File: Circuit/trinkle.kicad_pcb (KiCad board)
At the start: 2 copper layers, 13.6 x 23.2 mm, 12 parts, among them IC1 ATTINY84A-SS, P1 ISCP, P2 CONN_7, P3 CONN_7, SW1 RESET

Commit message: Photos and readme update
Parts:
- C2: value 10u -> 1u
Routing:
- net N-0000013: track 17.2 -> 17.9 mm
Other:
- board text added: "Trinkle ATTiny 84 Breakout - Version 1.1 Designed by John Spencer, 2014 https://github.com/mage0r/trinkle Made at hackmelbourne.org"
- board text removed: "Trinkle - ATTiny 84 Breakout Designed by John Spencer, 2014 https://github.com/mage0r/trinkle Version 1.0"
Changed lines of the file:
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@@
     (links 34)
     (no_connects 0)
-    (area 6.45 10.5264 27.3026 38)
+    (area 7.15 10.5264 27.3026 38.9)
     (thickness 1.6)
-    (drawings 25)
+    (drawings 27)
     (tracks 147)
     (zones 0)
@@
     (pad_to_mask_clearance 0)
     (aux_axis_origin 0 0)
-    (visible_elements FFFFFFBF)
+    (visible_elements 7FFFFFFF)
     (pcbplotparams
       (layerselection 284196865)
@@
       (effects (font (size 0.508 0.4572) (thickness 0.1143)))
     )
-    (fp_text value 10u (at 0 1 270) (layer F.SilkS)
+    (fp_text value 1u (at 0 1 270) (layer F.SilkS)
       (effects (font (size 0.4 0.4) (thickness 0.1)))
     )
@@
       (effects (font (size 0.7493 0.7493) (thickness 0.14986)))
     )
-    (fp_text value ATTINY84A-SS (at 0 1 90) (layer F.SilkS)
+    (fp_text value ATTINY84A-SS (at 0 0 90) (layer F.SilkS)
       (effects (font (size 0.7493 0.7493) (thickness 0.14986)))
     )
@@
     )
   )
-  (gr_text "Trinkle - ATTiny 84 Breakout\nDesigned by John Spencer, 2014\nhttps://github.com/mage0r/trinkle\nVersion 1.0" (at 20 35.2 270) (layer B.SilkS)
+  (gr_text +5V (at 21.9 35.2) (layer F.SilkS)
+    (effects (font (size 0.5 0.5) (thickness 0.125)))
+  )
+  (gr_text GND (at 16.5 35.2) (layer F.SilkS)
+    (effects (font (size 0.5 0.5) (thickness 0.125)))
+  )
+  (gr_text "Trinkle\nATTiny 84 Breakout - Version 1.1\nDesigned by John Spencer, 2014\nhttps://github.com/mage0r/trinkle\nMade at hackmelbourne.org\n" (at 20.7 35.3 270) (layer B.SilkS)
     (effects (font (size 0.5 0.5) (thickness 0.1)) (justify left mirror))
   )
@@
     (effects (font (size 0.5 0.5) (thickness 0.125)) (justify mirror))
   )
-  (gr_text "LED\nPWM\nD8" (at 21.1 23.9 90) (layer B.SilkS)
-    (effects (font (size 0.4 0.4) (thickness 0.1)) (justify mirror))
+  (gr_text "LED\nPWM\nD8" (at 21.3 23.9 90) (layer B.SilkS)
+    (effects (font (size 0.5 0.5) (thickness 0.1)) (justify mirror))
   )
   (gr_text D9 (at 22.4 29.1 90) (layer B.SilkS)
@@
   )
   (gr_text "SCL\nSCK\nA4" (at 17.3 21.4 270) (layer B.SilkS)
-    (effects (font (size 0.4 0.4) (thickness 0.1)) (justify mirror))
+    (effects (font (size 0.5 0.5) (thickness 0.1)) (justify mirror))
   )
   (gr_text A3 (at 16.1 23.9 270) (layer B.SilkS)
@@
   (segment (start 23.1366 19.9934) (end 23.1366 23.9951) (width 0.254) (layer F.Cu) (net 5))
   (segment (start 24.28 18.85) (end 23.1366 19.9934) (width 0.254) (layer F.Cu) (net 5))
-  (via (at 18.5342 21.7845) (size 0.889) (layers F.Cu B.Cu) (net 6))
+  (via (at 19.1 21.2) (size 0.889) (layers F.Cu B.Cu) (net 6))
   (segment (start 16.406 27.16) (end 17.4223 27.16) (width 0.254) (layer F.Cu) (net 6))
   (segment (start 16.5689 19.1011) (end 19.2 16.47) (width 0.254) (layer B.Cu) (net 6))
@@
   (segment (start 14.9981 21.39) (end 16.5689 19.8192) (width 0.254) (layer B.Cu) (net 6))
   (segment (start 14.12 21.39) (end 14.9981 21.39) (width 0.254) (layer B.Cu) (net 6))
-  (segment (start 16.5689 19.8192) (end 18.5342 21.7845) (width 0.254) (layer B.Cu) (net 6))
+  (segment (start 16.5689 19.8192) (end 19.1 21.2) (width 0.254) (layer B.Cu) (net 6))
   (segment (start 18.5342 26.0481) (end 17.4223 27.16) (width 0.254) (layer F.Cu) (net 6))
-  (segment (start 18.5342 21.7845) (end 18.5342 26.0481) (width 0.254) (layer F.Cu) (net 6))
+  (segment (start 19.1 21.2) (end 18.5342 26.0481) (width 0.254) (layer F.Cu) (net 6))
   (segment (start 16.406 25.1378) (end 16.406 25.89) (width 0.254) (layer F.Cu) (net 7))
   (segment (start 15.5166 24.2484) (end 16.406 25.1378) (width 0.254) (layer F.Cu) (net 7))

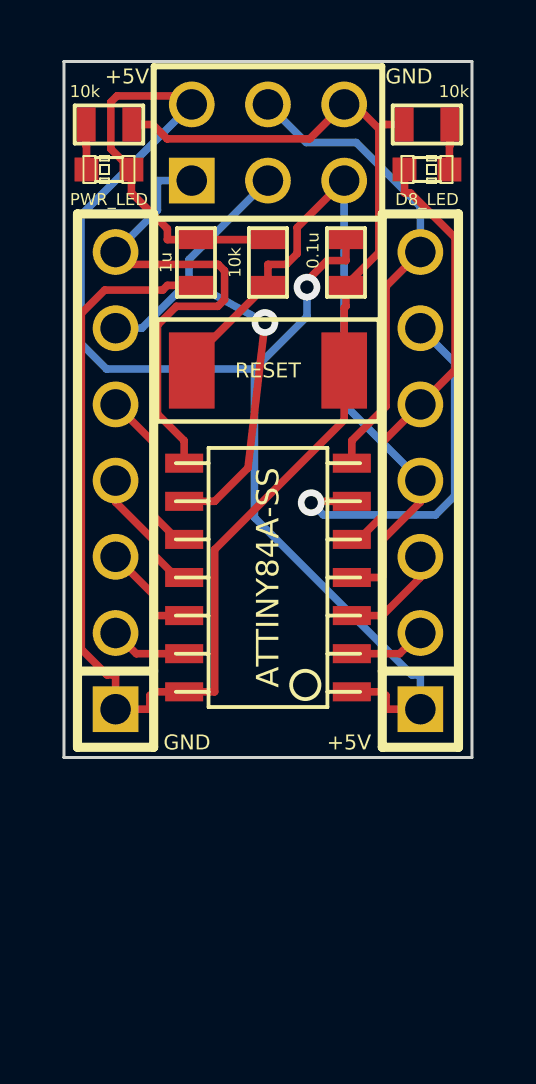
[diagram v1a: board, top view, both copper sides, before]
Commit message: Added usb port
Snap off capable usb port section
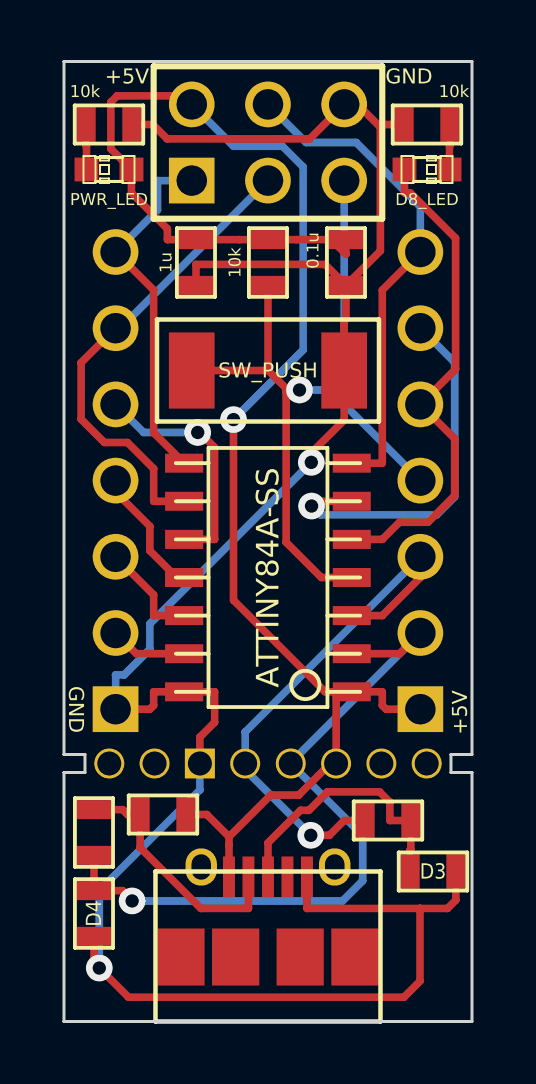
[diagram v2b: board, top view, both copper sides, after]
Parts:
- added CON1: USB-MINI-B, MINI_USB, F.Cu at (19.2, 42.0)
- added D3: DIODE, SM0603, F.Cu at (24.7, 39.5)
- added D4: DIODE, SM0603, F.Cu at (13.4, 40.9)
- added P4: CONN_4, breakaway, F.Cu at (19.2, 35.9)
- added R4: 1k, SM0603, F.Cu at (15.7, 37.6)
- added R5: 68, SM0603, F.Cu at (23.2, 37.8)
- added R6: 68, SM0603, F.Cu at (13.4, 38.2)
- P2, P3: footprint PIN_ARRAY-7X1 -> PIN_ARRAY-7X1_naked
- SW1: value RESET -> SW_PUSH
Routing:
- net GND: track 53.0 -> 75.9 mm, vias 0 -> 2
- net N-0000013: track 2.57 -> 24.2 mm, vias 0 -> 1
- net N-0000014: track 3.50 -> 18.1 mm, vias 0 -> 1
- net N-000009: track 0.00 -> 9.06 mm
- net N-0000010: track 0.00 -> 8.22 mm
- net N-0000019: track 16.5 -> 12.1 mm
- net +5V: track 49.8 -> 52.9 mm
- net N-0000021: track 5.58 -> 7.98 mm, vias 0 -> 1
- net N-0000015: track 24.7 -> 27.0 mm, vias 0 -> 1
- net N-0000020: track 17.9 -> 15.8 mm, vias 1 -> 0
- net N-0000016: track 14.7 -> 16.7 mm
- net N-0000018: track 16.0 -> 16.6 mm
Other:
- board size 13.6 x 23.2 mm -> 13.6 x 32 mm
- board text added: "Trinkle ATTiny 84 Breakout - Version 2.0 Designed by John Spencer, 2014 https://github.com/mage0r/trinkle Made at hackmelbourne.org"
- board text removed: "Trinkle ATTiny 84 Breakout - Version 1.1 Designed by John Spencer, 2014 https://github.com/mage0r/trinkle Made at hackmelbourne.org"
